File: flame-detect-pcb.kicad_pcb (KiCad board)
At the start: 2 copper layers, 82.5 x 101.6 mm, 48 parts, among them IC1 ATMEGA328-P, IC2 CH340G, Q1 MMBT2222, Q17 MMBT2222, Q2 MMBT2222, Q3 MMBT2907, Q4 MMBT2222, Q5 MMBT2907, Q6 MMBT2222, Q7 MMBT2222, T1 TRANSFORMER_(42TL013-RC), U1 NCV7805BDTRKG, X1 Crystal_GND2, X2 Crystal_GND2

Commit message: - Finished board layout.
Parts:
- moved C7 108.6 mm to (143.6, 99.3), turned to 270 degrees
- moved Q6 93.3 mm to (132.6, 53.8), turned to 270 degrees
- moved Q5 92.8 mm to (133.6, 115.3), turned to 270 degrees
- moved Q2 90.5 mm to (123.6, 110.8), turned to 90 degrees
- moved T1 82.0 mm to (162.6, 108.3)
- moved C8 81.6 mm to (143.6, 118.3), turned to 270 degrees
- moved Q1 81.2 mm to (123.6, 91.8), turned to 90 degrees
- moved Q7 78.8 mm to (139.1, 78.8), turned to 90 degrees
- moved R14 78.5 mm to (132.1, 47.3), turned to 90 degrees
- moved R15 77.6 mm to (160.1, 121.3), turned to 270 degrees
- moved R16 75.3 mm to (166.1, 119.3), turned to 180 degrees
- moved R13 72.1 mm to (128.1, 53.8), turned to 90 degrees
- moved Q3 71.8 mm to (133.6, 96.3), turned to 270 degrees
- moved R6 70.8 mm to (129.1, 92.3), turned to 270 degrees
- moved C5 70.5 mm to (121.6, 99.3), turned to 270 degrees
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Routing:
- net Net-(F1-Pad1): track 8.69 -> 134.8 mm
- net Net-(CONN_1-PadB6): track 0.00 -> 115.0 mm, vias 0 -> 2
- net Net-(C8-Pad1): track 0.00 -> 112.6 mm
- net Net-(C7-Pad1): track 0.95 -> 108.1 mm
- net Net-(C3-Pad1): track 0.00 -> 58.2 mm
- net Net-(CONN_1-PadB1): track 33.5 -> 85.3 mm
- net Net-(IC1-Pad17): track 0.00 -> 46.5 mm, vias 0 -> 2
- net Net-(CONN_1-PadA1): track 1.40 -> 41.8 mm
- net Net-(C4-Pad1): track 0.00 -> 38.3 mm
- net Net-(C5-Pad1): track 0.00 -> 19.3 mm
- net Net-(C6-Pad1): track 0.00 -> 19.1 mm
- net Net-(IC1-Pad6): track 0.28 -> 15.1 mm
- net +5V: track 128.0 -> 140.7 mm
- net Net-(IC1-Pad26): track 0.00 -> 11.1 mm
- net Net-(R15-Pad1): track 0.00 -> 9.53 mm
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
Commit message: - Finished footprints.
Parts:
- removed CONN_1: DEUTSCH_CONN_(DTM13-12PA-12PB-R008), flame-detect-pcb:DEUTSCH_CONN_(DTM13-12PA-12PB-R008)
- removed IC1: ATMEGA328-P, Housings_DIP:DIP-28_W7.62mm_LongPads
- removed IC2: CH340G, flame-detect-pcb:CH340G
- removed X1, X2: Crystal_GND2, flame-detect-pcb:RESONATOR_(CSTCE16M0V53C-R0)
- added C10: 0.1uF, Capacitors_SMD:C_0805, F.Cu at (75.7, 114.2)
- added C11: 0.1uF, Capacitors_SMD:C_0805, F.Cu at (67.9, 116.8)
- added C12: 10nF, Capacitors_SMD:C_0805, F.Cu at (179.4, 85.8)
- added C13: 10nF, Capacitors_SMD:C_0805, F.Cu at (183.6, 80.3)
- added C14: 1nF, Capacitors_SMD:C_0805, F.Cu at (179.6, 75.2)
- added C15: 1nF, Capacitors_SMD:C_0805, F.Cu at (175.4, 82.2)
- added C16: 10nF, Capacitors_SMD:C_0805, F.Cu at (179.4, 80.5)
- added C17: 10nF, Capacitors_SMD:C_0805, F.Cu at (183.6, 75.0)
- added C18: 1nF, Capacitors_SMD:C_0805, F.Cu at (187.1, 69.7)
- added C19: 1nF, Capacitors_SMD:C_0805, F.Cu at (183.2, 69.7)
- added C20: 10nF, Capacitors_SMD:C_0805, F.Cu at (184.1, 127.3)
- added C21: 10nF, Capacitors_SMD:C_0805, F.Cu at (179.6, 118.3)
- added C22: 1nF, Capacitors_SMD:C_0805, F.Cu at (187.4, 111.3)
- added C23: 1nF, Capacitors_SMD:C_0805, F.Cu at (176.2, 123.8)
- added C24: 10nF, Capacitors_SMD:C_0805, F.Cu at (172.2, 123.8)
- added C25: 10nF, Capacitors_SMD:C_0805, F.Cu at (183.7, 116.7)
- added C26: 1nF, Capacitors_SMD:C_0805, F.Cu at (180.1, 127.3)
- added C27: 1nF, Capacitors_SMD:C_0805, F.Cu at (183.6, 122.0)
- added C9: 22pF, Capacitors_SMD:C_0805, F.Cu at (82.1, 108.7)
- added CAN_HI_1: CONN_01X01, flame-detect-pcb:KEYSTONE_SPADE_TERM_(1287), F.Cu at (59.7, 112.1)
- added CAN_LO_1: CONN_01X01, flame-detect-pcb:KEYSTONE_SPADE_TERM_(1287), F.Cu at (70.6, 100.3)
- added CAN_TERM_1: CONN_01X02, Pin_Headers:Pin_Header_Straight_1x02_Pitch2.54mm_SMD_Pin1Left, F.Cu at (81.6, 101.6)
- added D10: BAV21W-7-F, Diodes_SMD:D_SOD-123, F.Cu at (158.3, 53.9)
- added D11: BZT52C5V1-TP, Diodes_SMD:D_SOD-123, F.Cu at (147.2, 53.9)
- added D12: BZT52C5V1-TP, Diodes_SMD:D_SOD-123, F.Cu at (137.1, 65.7)
- added D13: LED, LEDs:LED_1206, F.Cu at (165.5, 65.9)
- added D14: LED, LEDs:LED_1206, F.Cu at (150.6, 81.9)
- added D15: BAV21W-7-F, Diodes_SMD:D_SOD-123, F.Cu at (136.4, 119.6)
- added D16: BAV21W-7-F, Diodes_SMD:D_SOD-123, F.Cu at (136.4, 113.4)
- added D17: BZT52C5V1-TP, Diodes_SMD:D_SOD-123, F.Cu at (148.9, 107.7)
- added D18: BZT52C5V1-TP, Diodes_SMD:D_SOD-123, F.Cu at (137.1, 107.3)
- added D19: LED, LEDs:LED_1206, F.Cu at (168.1, 102.1)
- added D20: LED, LEDs:LED_1206, F.Cu at (176.3, 95.0)
- added D21: BAV21W-7-F, Diodes_SMD:D_SOD-123, F.Cu at (158.3, 95.4)
- added D22: BAV21W-7-F, Diodes_SMD:D_SOD-123, F.Cu at (160.0, 101.6)
- added D23: BZT52C5V1-TP, Diodes_SMD:D_SOD-123, F.Cu at (148.9, 101.6)
- added D24: BZT52C5V1-TP, Diodes_SMD:D_SOD-123, F.Cu at (147.2, 95.4)
- added D25: LED, LEDs:LED_1206, F.Cu at (165.5, 107.4)
- added D26: LED, LEDs:LED_1206, F.Cu at (150.6, 123.4)
- added D27: LED, LEDs:LED_1206, F.Cu at (76.6, 91.2)
- added D3: BAV21W-7-F, Diodes_SMD:D_SOD-123, F.Cu at (136.4, 71.9)
- added D4: BZT52C5V1-TP, Diodes_SMD:D_SOD-123, F.Cu at (148.9, 60.0)
- added D5: BZT52C5V1-TP, Diodes_SMD:D_SOD-123, F.Cu at (148.9, 66.2)
- added D6: LED, LEDs:LED_1206, F.Cu at (168.1, 60.5)
- added D7: LED, LEDs:LED_1206, F.Cu at (176.3, 53.5)
- added D8: BAV21W-7-F, Diodes_SMD:D_SOD-123, F.Cu at (160.0, 60.0)
- added DIO7: CONN_01X01, flame-detect-pcb:SPARE_THROUGH_HOLE, F.Cu at (89.0, 77.3)
- added DIO8: CONN_01X01, flame-detect-pcb:SPARE_THROUGH_HOLE, F.Cu at (78.5, 85.7)
- added DIO9: CONN_01X01, flame-detect-pcb:SPARE_THROUGH_HOLE, F.Cu at (106.5, 53.6)
- added FLAME_1: CONN_01X01, flame-detect-pcb:KEYSTONE_SPADE_TERM_(1287), F.Cu at (125.3, 66.0)
- added FLAME_2: CONN_01X01, flame-detect-pcb:KEYSTONE_SPADE_TERM_(1287), F.Cu at (125.3, 77.9)
- added FLAME_3: CONN_01X01, flame-detect-pcb:KEYSTONE_SPADE_TERM_(1287), F.Cu at (135.3, 54.2)
- added FLAME_4: CONN_01X01, flame-detect-pcb:KEYSTONE_SPADE_TERM_(1287), F.Cu at (125.3, 54.2)
- added FLAME_5: CONN_01X01, flame-detect-pcb:KEYSTONE_SPADE_TERM_(1287), F.Cu at (135.3, 95.7)
- added FLAME_6: CONN_01X01, flame-detect-pcb:KEYSTONE_SPADE_TERM_(1287), F.Cu at (125.3, 107.6)
- added FLAME_7: CONN_01X01, flame-detect-pcb:KEYSTONE_SPADE_TERM_(1287), F.Cu at (125.3, 119.4)
- added FLAME_8: CONN_01X01, flame-detect-pcb:KEYSTONE_SPADE_TERM_(1287), F.Cu at (125.3, 95.7)
- added GND_1: CONN_01X01, flame-detect-pcb:KEYSTONE_SPADE_TERM_(1287), F.Cu at (85.6, 54.2)
- added GND_2: CONN_01X01, flame-detect-pcb:KEYSTONE_SPADE_TERM_(1287), F.Cu at (67.8, 80.1)
- added ICSP_1: CONN_02X03, Pin_Headers:Pin_Header_Straight_2x03_Pitch2.54mm_SMD, F.Cu at (74.7, 70.9)
- added Q8: MMBT2907, TO_SOT_Packages_SMD:SOT-23, F.Cu at (135.3, 126.2)
- added R19: 1M, Resistors_SMD:R_0805, F.Cu at (171.6, 71.5)
- added R20: 240R, Resistors_SMD:R_0805, F.Cu at (164.2, 82.2)
- added R21: 240R, Resistors_SMD:R_0805, F.Cu at (179.7, 64.4)
- added R22: 470K, Resistors_SMD:R_0805, F.Cu at (167.7, 76.7)
- added R23: 470K, Resistors_SMD:R_0805, F.Cu at (159.1, 85.8)
- added R24: 5.1M, Resistors_SMD:R_0805, F.Cu at (187.4, 64.4)
- added R25: 5.1M, Resistors_SMD:R_0805, F.Cu at (175.7, 66.0)
- added R29: 1M, Resistors_SMD:R_0805, F.Cu at (179.8, 59.0)
- added R30: 13K, Resistors_SMD:R_0805, F.Cu at (171.6, 82.4)
- added R31: 1M, Resistors_SMD:R_0805, F.Cu at (168.0, 71.3)
- added R32: 13K, Resistors_SMD:R_0805, F.Cu at (172.7, 60.6)
- added R33: 3M, Resistors_SMD:R_0805, F.Cu at (176.3, 58.9)
- added R34: 3M, Resistors_SMD:R_0805, F.Cu at (155.2, 81.9)
- added R35: 1M, Resistors_SMD:R_0805, F.Cu at (164.4, 71.3)
- added R36: 1M, Resistors_SMD:R_0805, F.Cu at (181.0, 53.5)
- added R37: 240R, Resistors_SMD:R_0805, F.Cu at (159.9, 74.9)
- added R38: 240R, Resistors_SMD:R_0805, F.Cu at (175.5, 71.5)
- added R39: 470K, Resistors_SMD:R_0805, F.Cu at (159.9, 116.4)
- added R40: 470K, Resistors_SMD:R_0805, F.Cu at (181.3, 95.1)
- added R41: 5.1M, Resistors_SMD:R_0805, F.Cu at (164.6, 112.8)
- added R42: 5.1M, Resistors_SMD:R_0805, F.Cu at (155.4, 123.5)
- added R43: 1M, Resistors_SMD:R_0805, F.Cu at (159.6, 121.9)
- added R44: 13K, Resistors_SMD:R_0805, F.Cu at (168.4, 112.8)
- added R45: 1M, Resistors_SMD:R_0805, F.Cu at (185.2, 95.1)
- added R46: 13K, Resistors_SMD:R_0805, F.Cu at (177.0, 100.4)
- added R47: 3M, Resistors_SMD:R_0805, F.Cu at (171.9, 107.6)
- added R48: 3M, Resistors_SMD:R_0805, F.Cu at (180.5, 100.5)
- added R49: 1M, Resistors_SMD:R_0805, F.Cu at (163.8, 118.3)
- added R50: 1M, Resistors_SMD:R_0805, F.Cu at (175.5, 107.6)
- added R51: 240R, Resistors_SMD:R_0805, F.Cu at (159.5, 127.3)
- added R52: 240R, Resistors_SMD:R_0805, F.Cu at (179.4, 106.0)
- added R53: 470K, Resistors_SMD:R_0805, F.Cu at (173.1, 102.1)
- added R54: 470K, Resistors_SMD:R_0805, F.Cu at (168.0, 123.7)
- added R55: 5.1M, Resistors_SMD:R_0805, F.Cu at (176.4, 113.0)
- added R56: 5.1M, Resistors_SMD:R_0805, F.Cu at (172.1, 118.5)
- added R57: 1M, Resistors_SMD:R_0805, F.Cu at (183.3, 106.0)
- added R58: 13K, Resistors_SMD:R_0805, F.Cu at (186.8, 106.0)
- added R59: 1M, Resistors_SMD:R_0805, F.Cu at (180.1, 111.4)
- added R60: 13K, Resistors_SMD:R_0805, F.Cu at (183.6, 111.4)
- added R61: 3M, Resistors_SMD:R_0805, F.Cu at (175.8, 118.5)
- added R62: 3M, Resistors_SMD:R_0805, F.Cu at (187.6, 100.5)
- added R63: 1M, Resistors_SMD:R_0805, F.Cu at (184.1, 100.5)
- added R64: 1M, Resistors_SMD:R_0805, F.Cu at (167.4, 118.3)
- added R65: 240R, Resistors_SMD:R_0805, F.Cu at (172.3, 113.0)
- added R66: 240R, Resistors_SMD:R_0805, F.Cu at (163.8, 123.7)
- added R67: 1K, Resistors_SMD:R_0805, F.Cu at (113.5, 53.5)
- added SERIAL_1: CONN_01X04, Pin_Headers:Pin_Header_Straight_1x04_Pitch2.54mm_SMD_Pin1Left, F.Cu at (46.5, 75.4)
- added U2: LM358, Housings_SOIC:SOIC-8_3.9x4.9mm_Pitch1.27mm, F.Cu at (158.7, 67.7)
- added U3: LM358, Housings_SOIC:SOIC-8_3.9x4.9mm_Pitch1.27mm, F.Cu at (158.7, 109.2)
- added U4: LM358, Housings_SOIC:SOIC-8_3.9x4.9mm_Pitch1.27mm, F.Cu at (145.6, 115.4)
- added U5: LM3480-5.0, TO_SOT_Packages_SMD:SOT-23, F.Cu at (106.6, 60.0)
- added U6: ATMEGA328P-AU, Housings_QFP:TQFP-32_7x7mm_Pitch0.8mm, F.Cu at (75.1, 57.9)
- added U7: MCP2515T-I/SO, Housings_SOIC:SOIC-18W_7.5x11.6mm_Pitch1.27mm, F.Cu at (48.0, 104.9)
- added U8: MCP2551-I/SN, Housings_SOIC:SOIC-8_3.9x4.9mm_Pitch1.27mm, F.Cu at (60.4, 101.5)
- added U9: DIP_SW_3, Buttons_Switches_SMD:SW_DIP_x3_W8.61mm_Slide_LowProfile, F.Cu at (57.6, 74.9)
- added V_IN_1: CONN_01X01, flame-detect-pcb:KEYSTONE_SPADE_TERM_(1287), F.Cu at (85.6, 66.0)
- added V_IN_2: CONN_01X01, flame-detect-pcb:KEYSTONE_SPADE_TERM_(1287), F.Cu at (95.7, 54.2)
- added XTAL1: Crystal, Crystals:Crystal_SMD_HC49-SD, F.Cu at (48.5, 87.2)
- added XTAL2: Crystal, Crystals:Crystal_SMD_HC49-SD, F.Cu at (48.5, 117.3)
- C1, C2: footprint flame-detect-pcb:R_1206_HandSoldering_(narrow) -> Capacitors_SMD:C_0805; moved to F.Cu
- C3, C4: value 0.01uF -> 47uF; footprint flame-detect-pcb:R_1206_HandSoldering_(narrow) -> Capacitors_SMD:C_0805; moved to F.Cu
- C5: value 0.033uF -> 0.1uF; footprint flame-detect-pcb:R_1206_HandSoldering_(narrow) -> Capacitors_SMD:C_0805; moved to F.Cu
- C6: value 0.033uF -> 22pF; footprint flame-detect-pcb:R_1206_HandSoldering_(narrow) -> Capacitors_SMD:C_0805; moved to F.Cu
- C7, C8: value 10uF -> 22pF; footprint Capacitors_SMD:CP_Elec_4x4.5 -> Capacitors_SMD:C_0805; moved to F.Cu
- D1, D2: value 4148 -> BAV21W-7-F; footprint Diodes_SMD:D_SOD-323_HandSoldering -> Diodes_SMD:D_SOD-123; moved to F.Cu
- D9: moved to F.Cu
- F1: footprint Resistors_SMD:R_1812_HandSoldering -> Resistors_SMD:R_1812; moved to F.Cu
- Q1, Q2, Q4, Q6, Q7: value MMBT2222 -> MMBT2907; footprint TO_SOT_Packages_SMD:SOT-23_Handsoldering -> TO_SOT_Packages_SMD:SOT-23; moved to F.Cu
- Q17, Q3, Q5: footprint TO_SOT_Packages_SMD:SOT-23_Handsoldering -> TO_SOT_Packages_SMD:SOT-23; moved to F.Cu
- R1: value 500k -> 5.1K; footprint flame-detect-pcb:R_1206_HandSoldering_(narrow) -> Resistors_SMD:R_0805; moved to F.Cu
- R10, R12, R18: value 10k -> 1M; footprint flame-detect-pcb:R_1206_HandSoldering_(narrow) -> Resistors_SMD:R_0805; moved to F.Cu
- R11, R13: value 10k -> 13K; footprint flame-detect-pcb:R_1206_HandSoldering_(narrow) -> Resistors_SMD:R_0805; moved to F.Cu
- R14, R17: value 10k -> 3M; footprint flame-detect-pcb:R_1206_HandSoldering_(narrow) -> Resistors_SMD:R_0805; moved to F.Cu
- R15, R16, R27, R28: footprint flame-detect-pcb:R_1206_HandSoldering_(narrow) -> Resistors_SMD:R_0805; moved to F.Cu
- R2: value 500k -> 560R; footprint flame-detect-pcb:R_1206_HandSoldering_(narrow) -> Resistors_SMD:R_0805; moved to F.Cu
- R26: value 680 -> 680R; footprint flame-detect-pcb:R_1206_HandSoldering_(narrow) -> Resistors_SMD:R_0805; moved to F.Cu
- R3, R4: value 10M -> 10K; footprint flame-detect-pcb:R_1206_HandSoldering_(narrow) -> Resistors_SMD:R_0805; moved to F.Cu
- R5: value 100k -> 120R; footprint flame-detect-pcb:R_1206_HandSoldering_(narrow) -> Resistors_SMD:R_0805; moved to F.Cu
- R6, R7: value 10k -> 470K; footprint flame-detect-pcb:R_1206_HandSoldering_(narrow) -> Resistors_SMD:R_0805; moved to F.Cu
- R8: value 10k -> 5.1M; footprint flame-detect-pcb:R_1206_HandSoldering_(narrow) -> Resistors_SMD:R_0805; moved to F.Cu
- R9: value 100k -> 5.1M; footprint flame-detect-pcb:R_1206_HandSoldering_(narrow) -> Resistors_SMD:R_0805; moved to F.Cu
- U1: value NCV7805BDTRKG -> LM358; footprint flame-detect-pcb:REGULATOR_(NCV7805BDTRKG) -> Housings_SOIC:SOIC-8_3.9x4.9mm_Pitch1.27mm; moved to F.Cu
- moved F1 120.2 mm to (59.3, 85.3), turned to 0 degrees
- moved T1 118.6 mm to (55.1, 58.4)
- moved C1 91.7 mm to (69.8, 91.2)
- moved C2 88.3 mm to (65.3, 91.2), turned to 0 degrees
- moved R27 87.9 mm to (65.4, 70.9), turned to 0 degrees
- moved D9 82.9 mm to (96.6, 64.3), turned to 0 degrees
- moved R16 81.5 mm to (99.5, 72.3), turned to 0 degrees
- moved R15 80.7 mm to (96.0, 72.3), turned to 0 degrees
- moved R9 80.5 mm to (183.6, 59.0), turned to 0 degrees
- moved Q6 73.2 mm to (143.6, 126.2), turned to 0 degrees
- moved Q17 73.1 mm to (88.3, 83.7)
- moved Q2 72.6 mm to (169.3, 54.4), turned to 0 degrees
- moved C8 71.4 mm to (72.2, 119.5), turned to 0 degrees
- moved R12 63.7 mm to (179.4, 69.9), turned to 0 degrees
- moved R5 59.1 mm to (71.3, 111.5), turned to 0 degrees
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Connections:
- net Net-(C2-Pad1) renamed RST
- C1 pad 1: +5V -> 5V
- C3 pad 1: Net-(C3-Pad1) -> VBATT
- C4 pad 1: Net-(C4-Pad1) -> 5V
- C5 pad 1: Net-(C5-Pad1) -> 5V
- C6 pad 1: Net-(C6-Pad1) -> GND
- C6 pad 2: GND -> Net-(C6-Pad2)
- C7 pad 1: Net-(C7-Pad1) -> GND
- C7 pad 2: GND -> Net-(C7-Pad2)
- D1 pad 1: Net-(C5-Pad1) -> Net-(D1-Pad1)
- D2 pad 1: Net-(C6-Pad1) -> Net-(D2-Pad1)
- D2 pad 2: GND -> Net-(C12-Pad1)
- F1 pad 1: Net-(F1-Pad1) -> VBATT
- Q1 pad 1: Net-(C5-Pad1) -> Net-(Q1-Pad1)
- Q1 pad 2: GND -> Net-(Q1-Pad2)
- Q1 pad 3: Net-(Q1-Pad3) -> Net-(D2-Pad1)
- Q17 pad 3: Net-(Q17-Pad3) -> Net-(D1-Pad1)
- Q2 pad 1: Net-(C6-Pad1) -> Net-(Q2-Pad1)
- Q2 pad 2: GND -> Net-(Q2-Pad2)
- Q2 pad 3: Net-(Q2-Pad3) -> Net-(D3-Pad1)
- Q3 pad 2: Net-(F1-Pad1) -> Net-(Q3-Pad2)
- Q3 pad 3: Net-(C7-Pad1) -> Net-(D8-Pad1)
- Q4 pad 2: GND -> Net-(Q4-Pad2)
- Q4 pad 3: Net-(IC1-Pad25) -> Net-(D10-Pad1)
- Q5 pad 2: Net-(F1-Pad1) -> Net-(Q5-Pad2)
- Q5 pad 3: Net-(C8-Pad1) -> Net-(D15-Pad1)
- Q6 pad 2: GND -> Net-(Q6-Pad2)
- Q6 pad 3: Net-(IC1-Pad26) -> Net-(D16-Pad1)
- Q7 pad 2: GND -> Net-(Q7-Pad2)
- Q7 pad 3: Net-(IC1-Pad6) -> Net-(D21-Pad1)
- R1 pad 1: Net-(C5-Pad1) -> V_REF
- R1 pad 2: Net-(C3-Pad1) -> VBATT
- R10 pad 1: Net-(Q2-Pad3) -> Net-(C14-Pad2)
- R10 pad 2: Net-(Q5-Pad1) -> Net-(Q1-Pad1)
- R11 pad 1: GND -> Net-(R11-Pad1)
- R11 pad 2: Net-(C7-Pad1) -> V_REF
- R12 pad 1: GND -> Net-(C15-Pad2)
- R12 pad 2: Net-(C8-Pad1) -> Net-(Q2-Pad1)
- R13 pad 1: Net-(IC1-Pad26) -> Net-(R13-Pad1)
- R13 pad 2: +5V -> V_REF
- R14 pad 1: Net-(Q6-Pad1) -> Net-(FLAME_1-Pad1)
- R14 pad 2: Net-(C8-Pad1) -> Net-(C14-Pad2)
- R15 pad 2: Net-(CONN_1-PadA1) -> PULSE
- R17 pad 1: Net-(IC1-Pad6) -> Net-(FLAME_2-Pad1)
- R17 pad 2: +5V -> Net-(C15-Pad2)
- R18 pad 1: Net-(Q7-Pad1) -> AI0
- R18 pad 2: Net-(CONN_1-PadB6) -> Net-(R11-Pad1)
- R2 pad 1: Net-(C6-Pad1) -> GND
- R2 pad 2: Net-(C4-Pad1) -> V_REF
- R27 pad 1: Net-(IC1-Pad10) -> Net-(C7-Pad2)
- R27 pad 2: Net-(IC1-Pad9) -> Net-(C6-Pad2)
- R28 pad 1: +5V -> 5V
- R3 pad 1: GND -> 5V
- R3 pad 2: Net-(C5-Pad1) -> Net-(R3-Pad2)
- R4 pad 2: Net-(C6-Pad1) -> Net-(R4-Pad2)
- R5 pad 1: Net-(Q3-Pad1) -> Net-(CAN_LO_1-Pad1)
- R5 pad 2: Net-(F1-Pad1) -> Net-(CAN_TERM_1-Pad2)
- R6 pad 1: Net-(Q1-Pad3) -> PULSE
- R6 pad 2: Net-(Q3-Pad1) -> Net-(Q1-Pad2)
- R7 pad 1: Net-(IC1-Pad25) -> PULSE
- R7 pad 2: +5V -> Net-(Q2-Pad2)
- R8 pad 1: Net-(Q4-Pad1) -> Net-(C12-Pad1)
- R8 pad 2: Net-(C7-Pad1) -> GND
- R9 pad 1: Net-(Q5-Pad1) -> Net-(C13-Pad1)
- R9 pad 2: Net-(F1-Pad1) -> GND
- T1 pad 4: Net-(F1-Pad1) -> VBATT
- T1 pad 6: Net-(Q17-Pad3) -> Net-(D1-Pad1)
- U1 pad 1: Net-(F1-Pad1) -> AI0
- U1 pad 2: GND -> Net-(R11-Pad1)
- U1 pad 3: +5V -> Net-(C12-Pad1)
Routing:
- net +5V: track 140.7 -> 0.00 mm
- net Net-(F1-Pad1): track 134.8 -> 0.00 mm
- net D+: track 127.1 -> 0.00 mm
- net D-: track 122.6 -> 0.00 mm
- net Net-(CONN_1-PadB6): track 115.0 -> 0.00 mm, vias 2 -> 0
- net Net-(C8-Pad1): track 112.6 -> 0.00 mm
- net Net-(C7-Pad1): track 108.1 -> 0.00 mm
- net Net-(D9-Pad2): track 85.3 -> 0.00 mm
- net Net-(C3-Pad1): track 58.2 -> 0.00 mm
- net Net-(R26-Pad2): track 46.5 -> 0.00 mm, vias 2 -> 0
- net Net-(CONN_1-PadA1): track 41.8 -> 0.00 mm
- net RXD: track 40.9 -> 0.00 mm, vias 2 -> 0
- net TXD: track 39.5 -> 0.00 mm, vias 2 -> 0
- net Net-(C4-Pad1): track 38.3 -> 0.00 mm
- net RST: track 29.3 -> 0.00 mm
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- removed copper zone on B.Cu, net GND
- removed copper zone on F.Cu, net GND
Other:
- board outline removed

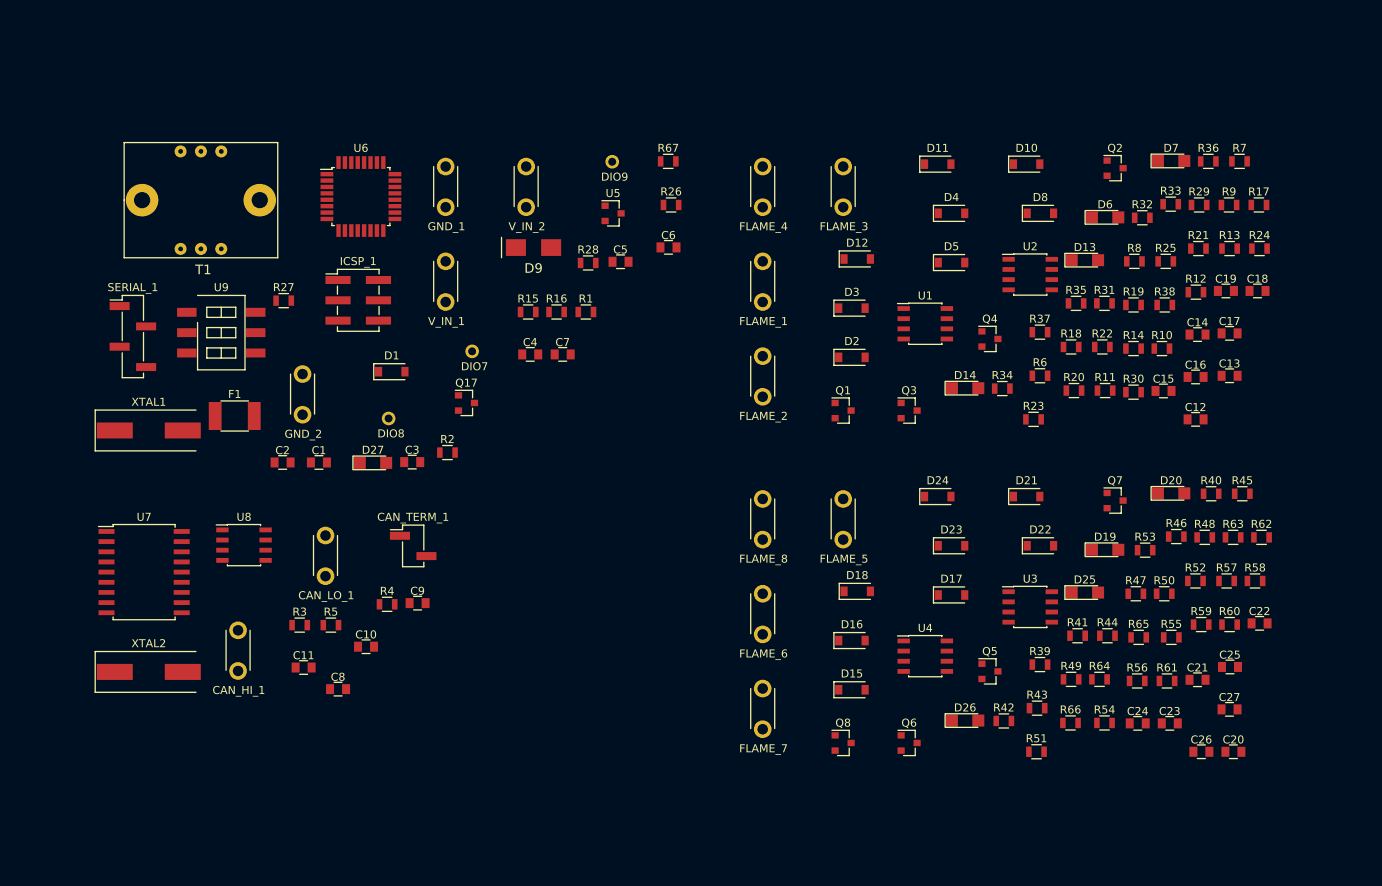
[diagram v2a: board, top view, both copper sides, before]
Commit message: - Finished PCB layout.
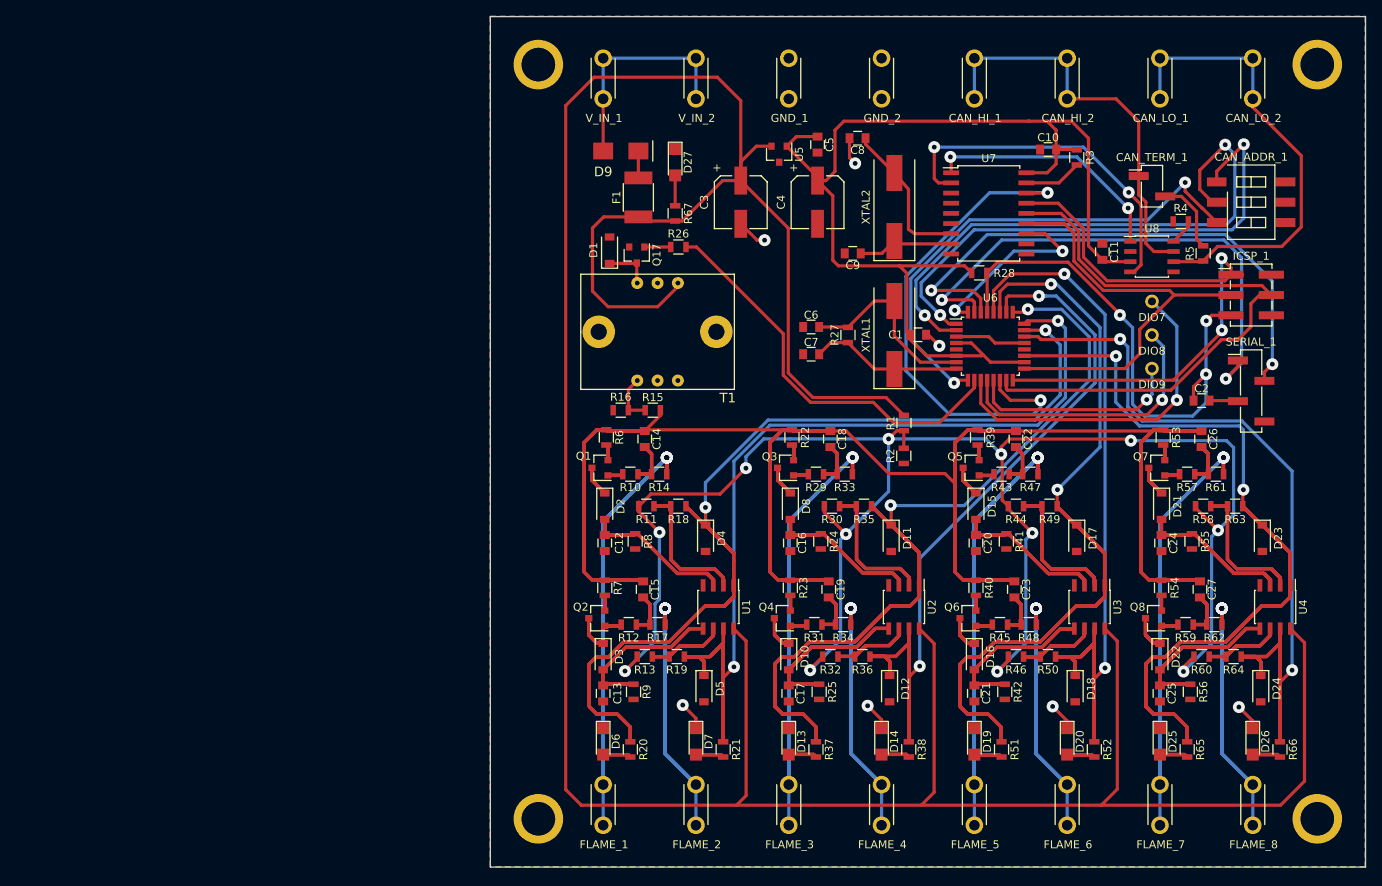
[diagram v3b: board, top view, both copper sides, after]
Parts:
- removed U9: DIP_SW_3, Buttons_Switches_SMD:SW_DIP_x3_W8.61mm_Slide_LowProfile
- added CAN_ADDR_1: DIP_SW_3, Buttons_Switches_SMD:SW_DIP_x3_W8.61mm_Slide_LowProfile, F.Cu at (186.3, 58.6)
- added CAN_HI_2: CONN_01X01, flame-detect-pcb:KEYSTONE_SPADE_TERM_(1287), F.Cu at (163.3, 40.6)
- added CAN_LO_2: CONN_01X01, flame-detect-pcb:KEYSTONE_SPADE_TERM_(1287), F.Cu at (186.5, 40.6)
- added GND_3: CONN_01X01, flame-detect-pcb:PEM_STANDOFF_THRU_(SMTSOB-116-12ET), F.Cu at (97.2, 135.7)
- added GND_4: CONN_01X01, flame-detect-pcb:PEM_STANDOFF_THRU_(SMTSOB-116-12ET), F.Cu at (97.2, 41.4)
- added GND_5: CONN_01X01, flame-detect-pcb:PEM_STANDOFF_THRU_(SMTSOB-116-12ET), F.Cu at (194.6, 41.4)
- added GND_6: CONN_01X01, flame-detect-pcb:PEM_STANDOFF_THRU_(SMTSOB-116-12ET), F.Cu at (194.6, 135.7)
- C3, C4: footprint Capacitors_SMD:C_0805 -> Capacitors_SMD:CP_Elec_6.3x5.3
- moved SERIAL_1 140.0 mm to (186.3, 82.2)
- moved CAN_LO_1 120.2 mm to (174.9, 40.6)
- moved U8 119.1 mm to (173.9, 65.4)
- moved R5 118.5 mm to (180.3, 65.0), turned to 90 degrees
- moved CAN_HI_1 116.6 mm to (151.7, 40.6)
- moved C2 115.1 mm to (180.1, 83.4)
- moved U7 114.7 mm to (153.5, 60.0)
- moved R3 113.4 mm to (164.5, 53.0), turned to 270 degrees
- moved C11 112.6 mm to (167.7, 64.8), turned to 270 degrees
- moved ICSP_1 111.6 mm to (186.3, 70.2)
- moved R4 110.1 mm to (177.5, 61.0)
- moved XTAL2 109.8 mm to (141.7, 59.2), turned to 90 degrees
- moved C10 105.5 mm to (160.9, 52.0)
- moved CAN_TERM_1 102.7 mm to (173.9, 56.6)
- moved R9 96.1 mm to (109.1, 119.8), turned to 270 degrees
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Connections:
- ICSP_1 pad 2: 5V -> Net-(ICSP_1-Pad2)
- T1 pad 7: (no net) -> GND
- T1 pad 8: (no net) -> GND
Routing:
- net PULSE: track 0.00 -> 575.3 mm
- net VBATT: track 0.00 -> 397.0 mm
- net AI0: track 0.00 -> 260.6 mm, vias 0 -> 2
- net AI2: track 0.00 -> 245.5 mm, vias 0 -> 2
- net AI6: track 0.00 -> 239.2 mm, vias 0 -> 2
- net AI4: track 0.00 -> 237.2 mm, vias 0 -> 2
- net V_REF: track 0.00 -> 222.5 mm, vias 0 -> 12
- net Net-(FLAME_7-Pad1): track 0.00 -> 190.0 mm, vias 0 -> 4
- net Net-(FLAME_5-Pad1): track 0.00 -> 190.0 mm, vias 0 -> 4
- net Net-(FLAME_3-Pad1): track 0.00 -> 190.0 mm, vias 0 -> 4
- net Net-(FLAME_1-Pad1): track 0.00 -> 190.0 mm, vias 0 -> 4
- net AI1: track 0.00 -> 183.6 mm, vias 0 -> 2
- net AI7: track 0.00 -> 168.9 mm, vias 0 -> 2
- net AI3: track 0.00 -> 164.5 mm, vias 0 -> 2
- net AI5: track 0.00 -> 162.7 mm, vias 0 -> 2
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- added copper zone on B.Cu, net GND
- added copper zone on F.Cu, net GND
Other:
- board outline added: 109.4 x 106.3 mm

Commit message: - Fixed a couple layout issues, then created gerbers.
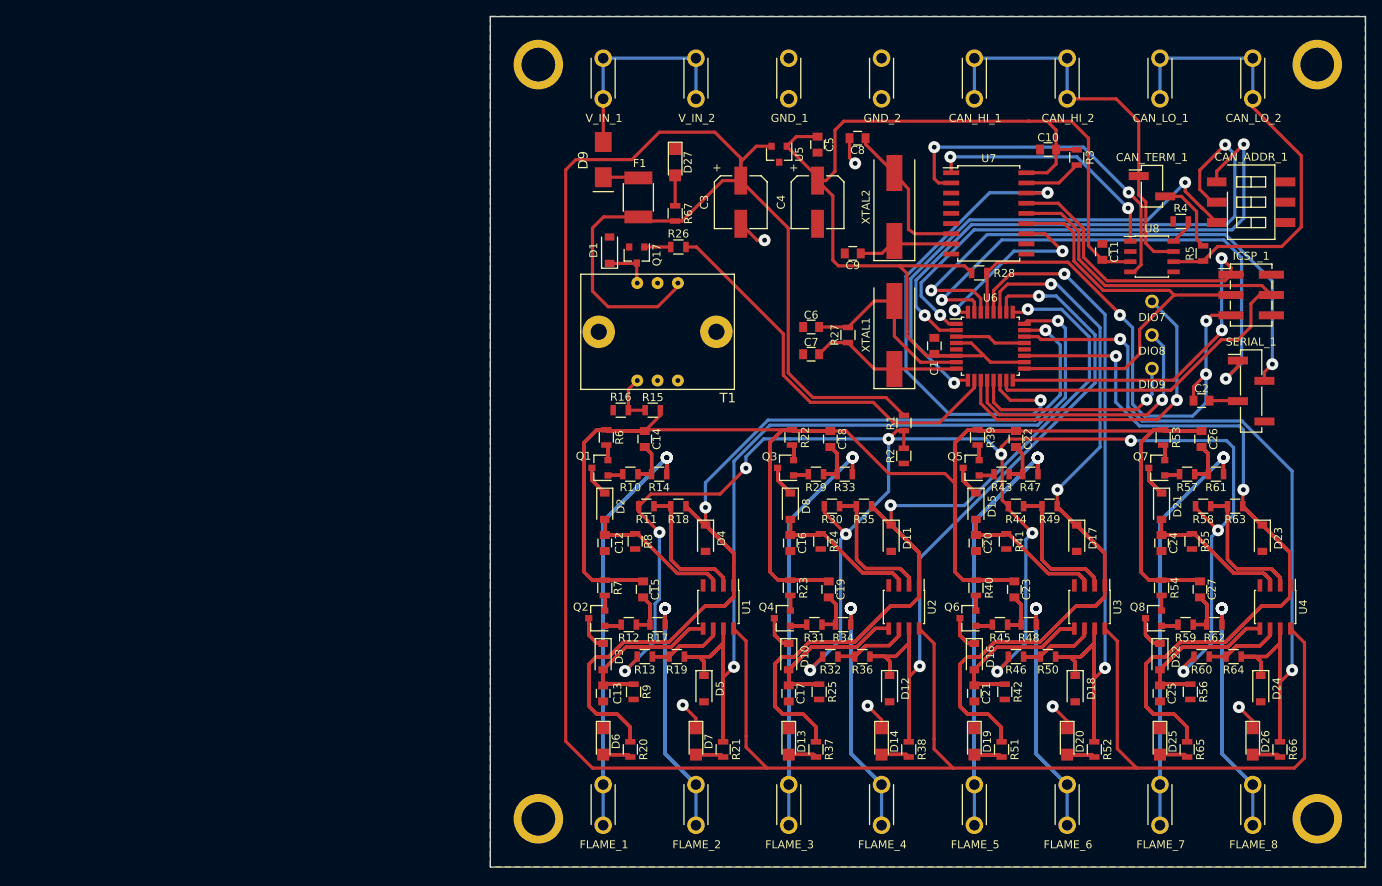
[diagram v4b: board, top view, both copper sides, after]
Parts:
- moved C1 2.47 mm to (146.7, 76.6), turned to 90 degrees
- moved D9 2.43 mm to (105.3, 53.3), turned to 90 degrees
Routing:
- net VBATT: track 397.0 -> 360.5 mm
- net 5V: track 141.3 -> 144.1 mm
- net GND: track 32.3 -> 30.1 mm, vias 7 -> 6
- net Net-(D9-Pad2): track 28.3 -> 27.2 mm
- net Net-(D9-Pad1): track 3.36 -> 4.42 mm

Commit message: - Fixed several bugs.
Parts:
- added C28: 0.1uF, Capacitors_SMD:C_0805, F.Cu at (161.2, 77.8)
- CAN_TERM_1: footprint Pin_Headers:Pin_Header_Straight_1x02_Pitch2.54mm_SMD_Pin1Left -> Pin_Headers:Pin_Header_Straight_1x02_Pitch2.54mm_SMD_Pin1Right
- D9: footprint flame-detect-pcb:SCHOTTKY_(PMEG3030EP,115) -> flame-detect-pcb:DO-214AB
- R18, R19, R35, R36, R49, R50, R63, R64: value 1M -> 10K
- SERIAL_1: footprint Pin_Headers:Pin_Header_Straight_1x04_Pitch2.54mm_SMD_Pin1Left -> Pin_Headers:Pin_Header_Straight_1x04_Pitch2.54mm_SMD_Pin1Right
- moved CAN_HI_2 11.6 mm to (174.9, 40.6)
- moved CAN_LO_1 11.6 mm to (163.3, 40.6)
- moved D27 2.00 mm to (116.3, 53.7)
- moved R67 2.00 mm to (116.3, 60.1)
- moved F1 1.67 mm to (111.4, 58.0)
- moved D9 1.30 mm to (105.3, 54.6)
- turned D10 to 90 degrees
- turned D15 to 90 degrees
- turned D16 to 90 degrees
- turned D2 to 90 degrees
- turned D21 to 90 degrees
- turned D22 to 90 degrees
- turned D3 to 90 degrees
- turned D8 to 90 degrees
- turned R4 to 180 degrees
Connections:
- D10 pad 1: Net-(D10-Pad1) -> Net-(C17-Pad1)
- D10 pad 2: Net-(C17-Pad1) -> Net-(D10-Pad2)
- D15 pad 1: Net-(D15-Pad1) -> Net-(C20-Pad1)
- D15 pad 2: Net-(C20-Pad1) -> Net-(D15-Pad2)
- D16 pad 1: Net-(D16-Pad1) -> Net-(C21-Pad1)
- D16 pad 2: Net-(C21-Pad1) -> Net-(D16-Pad2)
- D2 pad 1: Net-(D2-Pad1) -> Net-(C12-Pad1)
- D2 pad 2: Net-(C12-Pad1) -> Net-(D2-Pad2)
- D21 pad 1: Net-(D21-Pad1) -> Net-(C24-Pad1)
- D21 pad 2: Net-(C24-Pad1) -> Net-(D21-Pad2)
- D22 pad 1: Net-(D22-Pad1) -> Net-(C25-Pad1)
- D22 pad 2: Net-(C25-Pad1) -> Net-(D22-Pad2)
- D3 pad 1: Net-(D3-Pad1) -> Net-(C13-Pad1)
- D3 pad 2: Net-(C13-Pad1) -> Net-(D3-Pad2)
- D8 pad 1: Net-(D8-Pad1) -> Net-(C16-Pad1)
- D8 pad 2: Net-(C16-Pad1) -> Net-(D8-Pad2)
- ICSP_1 pad 2: Net-(ICSP_1-Pad2) -> 5V
- Q1 pad 3: Net-(D2-Pad1) -> Net-(D2-Pad2)
- Q2 pad 3: Net-(D3-Pad1) -> Net-(D3-Pad2)
- Q3 pad 3: Net-(D8-Pad1) -> Net-(D8-Pad2)
- Q4 pad 3: Net-(D10-Pad1) -> Net-(D10-Pad2)
- Q5 pad 3: Net-(D15-Pad1) -> Net-(D15-Pad2)
- Q6 pad 3: Net-(D16-Pad1) -> Net-(D16-Pad2)
- Q7 pad 3: Net-(D21-Pad1) -> Net-(D21-Pad2)
- Q8 pad 3: Net-(D22-Pad1) -> Net-(D22-Pad2)
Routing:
- net 5V: track 144.1 -> 195.5 mm, vias 0 -> 2
- net Net-(D3-Pad2): track 0.00 -> 17.3 mm
- net Net-(D3-Pad1): track 17.3 -> 0.00 mm
- net Net-(D10-Pad2): track 0.00 -> 17.3 mm
- net Net-(D10-Pad1): track 17.3 -> 0.00 mm
- net Net-(D22-Pad2): track 0.00 -> 17.3 mm
- net Net-(D22-Pad1): track 17.3 -> 0.00 mm
- net Net-(D16-Pad2): track 0.00 -> 17.3 mm
- net Net-(D16-Pad1): track 17.3 -> 0.00 mm
- net Net-(D2-Pad2): track 0.00 -> 15.3 mm
- net Net-(D2-Pad1): track 15.3 -> 0.00 mm
- net Net-(D21-Pad2): track 0.00 -> 15.3 mm
- net Net-(D21-Pad1): track 15.3 -> 0.00 mm
- net Net-(D8-Pad2): track 0.00 -> 15.3 mm
- net Net-(D8-Pad1): track 15.3 -> 0.00 mm
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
